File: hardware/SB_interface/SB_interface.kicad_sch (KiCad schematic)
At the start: 33 parts, among them J1 8P8C_TelPairs, J2 8P8C_TelPairs, J3 8P8C_TelPairs, J4 Screw_Terminal_01x02, J5 Screw_Terminal_01x02, J6 Conn_01x10_Pin, J7 Jack-DC, K1 J104D2C12VDC.36S, Q1 2N7002, U1 MCP23017_SP, U2 MCP23017_SP

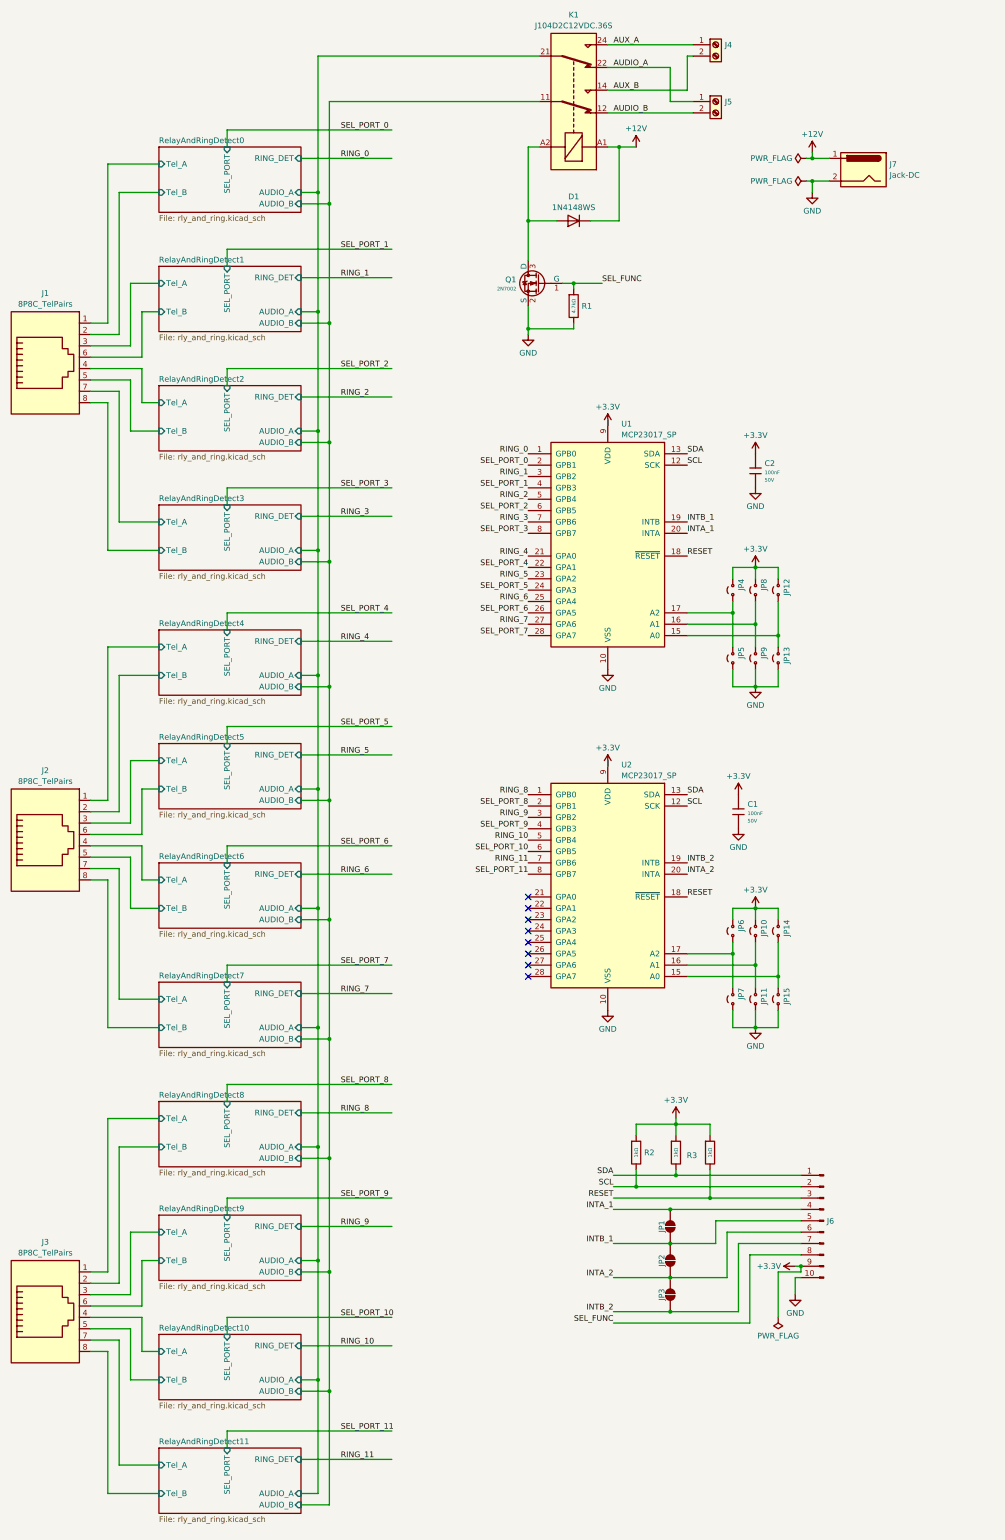
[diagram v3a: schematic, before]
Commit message: layout of tel inputs
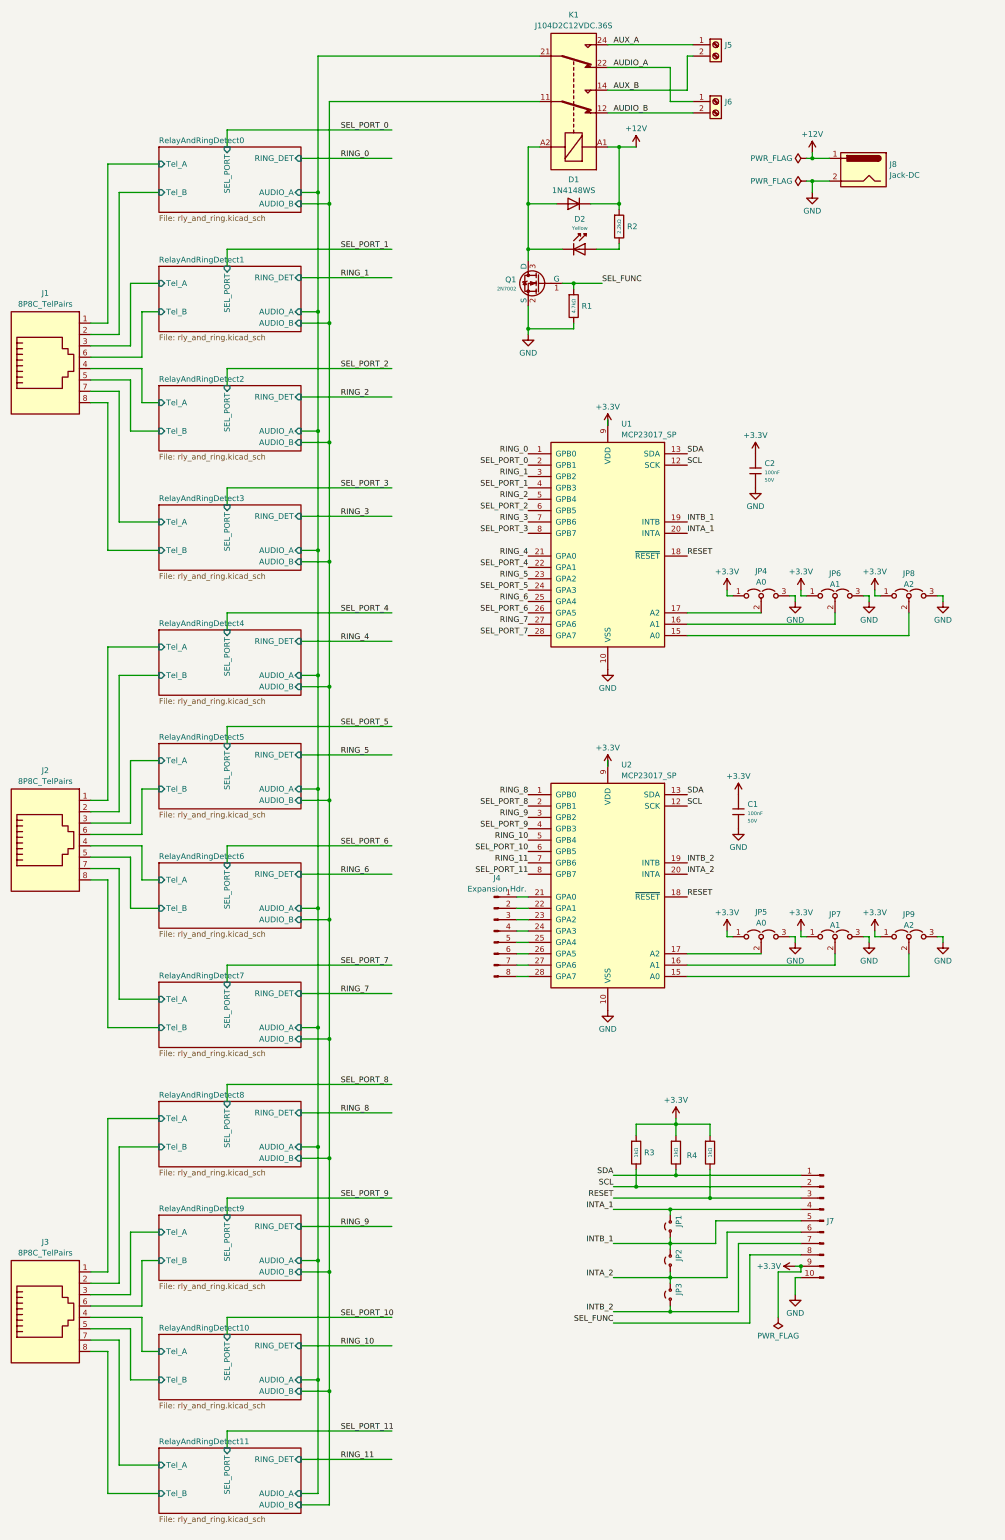
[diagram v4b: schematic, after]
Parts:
- removed JP1, JP2, JP3: SolderJumper_2_Open, Jumper:SolderJumper-2_P1.3mm_Open_Pad1.0x1.5mm, symbol Jumper:SolderJumper_2_Open
- removed JP10, JP11, JP12, JP13, JP14, JP15, JP4, JP5, JP6, JP7, JP8, JP9: Jumper_2_Small_Open, Connector_PinHeader_2.54mm:PinHeader_1x02_P2.54mm_Vertical, symbol Jumper:Jumper_2_Small_Open
- added D2: Yellow, PCM_JLCPCB:D_0805, symbol PCM_JLCPCB-Diodes:LED,0805,Yellow
- added J4: Expansion Hdr., Connector_PinHeader_2.54mm:PinHeader_1x08_P2.54mm_Vertical, symbol Connector:Conn_01x08_Pin
- added JP1, JP2, JP3: Jumper_2_Small_Open, Connector_PinHeader_2.54mm:PinHeader_1x02_P2.54mm_Vertical, symbol Jumper:Jumper_2_Small_Open
- added JP4, JP5: A0, Connector_PinHeader_2.54mm:PinHeader_1x03_P2.54mm_Vertical, symbol Jumper:Jumper_3_Open
- added JP6, JP7: A1, Connector_PinHeader_2.54mm:PinHeader_1x03_P2.54mm_Vertical, symbol Jumper:Jumper_3_Open
- added JP8, JP9: A2, Connector_PinHeader_2.54mm:PinHeader_1x03_P2.54mm_Vertical, symbol Jumper:Jumper_3_Open
- added R2: 2.2kΩ, PCM_JLCPCB:R_0805, symbol PCM_JLCPCB-Resistors:0805,2.2kΩ
- renumbered J4 to J5, J5 to J6, J6 to J7, J7 to J8, R2 to R3, R3 to R4, R4 to R5
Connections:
- net +12V: now also R2.1
- net +3.3V: now also JP4.1 (A), JP5.1 (A), JP6.1 (A), JP7.1 (A), JP8.1 (A), JP9.1 (A)
- net GND: now also JP4.3 (B), JP5.3 (B), JP6.3 (B), JP7.3 (B), JP8.3 (B), JP9.3 (B)
- net INTA_1: now also JP1.2 (B)
- net INTA_2: now also JP2.1 (A), JP3.2 (B)
- net INTB_1: now also JP1.1 (A), JP2.2 (B)
- net INTB_2: now also JP3.1 (A)
- net at U2.15 (A0): now also JP9.2 (C)
- net at U2.17 (A2): now also JP5.2 (C)
- net at D1.2 (A), K1.A2, Q1.3 (D): now also D2.1
- net at U2.16 (A1): now also JP7.2 (C)
- net at U2.21 (GPA0): now also J4.1 (Pin_1)
- net at U2.22 (GPA1): now also J4.2 (Pin_2)
- net at U2.23 (GPA2): now also J4.3 (Pin_3)
- net at U2.24 (GPA3): now also J4.4 (Pin_4)
- net at U2.25 (GPA4): now also J4.5 (Pin_5)
- net at U2.26 (GPA5): now also J4.6 (Pin_6)
- net at U2.27 (GPA6): now also J4.7 (Pin_7)
- net at U2.28 (GPA7): now also J4.8 (Pin_8)
- net at U1.15 (A0): now also JP8.2 (C)
- net at U1.17 (A2): now also JP4.2 (C)
- net at U1.16 (A1): now also JP6.2 (C)
- new net: D2.2, R2.2
- no-connect marks 8 -> 0
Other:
- moved on the sheet: D1

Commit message: more layout stuff
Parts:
- removed J4: Expansion Hdr., Connector_PinHeader_2.54mm:PinHeader_1x08_P2.54mm_Vertical, symbol Connector:Conn_01x08_Pin
- removed J7: Conn_01x10_Pin, Connector_PinHeader_2.54mm:PinHeader_1x10_P2.54mm_Vertical, symbol Connector:Conn_01x10_Pin
- removed JP1, JP2, JP3: Jumper_2_Small_Open, Connector_PinHeader_2.54mm:PinHeader_1x02_P2.54mm_Vertical, symbol Jumper:Jumper_2_Small_Open
- added J4: Conn_01x09_Pin, Connector_PinHeader_2.54mm:PinHeader_1x09_P2.54mm_Vertical, symbol Connector:Conn_01x09_Pin
- added J7: EXTENSION HDR., Connector_PinHeader_2.54mm:PinHeader_1x07_P2.54mm_Vertical, symbol Connector:Conn_01x07_Pin
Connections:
- net +3.3V: now also J4.1 (Pin_1)
- net GND: now also J4.9 (Pin_9)
- net INTA_1: now also J4.4 (Pin_4)
- net INTA_2: now also J4.8 (Pin_8)
- net INTB_1: now also J4.5 (Pin_5)
- net INTB_2: now also J4.7 (Pin_7)
- net RESET: now also J4.6 (Pin_6)
- net RING_4: now also U1.27 (GPA6); no longer U1.21 (GPA0)
- net RING_5: now also U1.25 (GPA4); no longer U1.23 (GPA2)
- net RING_6: now also U1.23 (GPA2); no longer U1.25 (GPA4)
- net RING_7: now also U1.21 (GPA0); no longer U1.27 (GPA6)
- net SCL: now also J4.2 (Pin_2)
- net SDA: now also J4.3 (Pin_3)
- net SEL_FUNC: now also U2.28 (GPA7)
- net SEL_PORT_4: now also U1.28 (GPA7); no longer U1.22 (GPA1)
- net SEL_PORT_5: now also U1.26 (GPA5); no longer U1.24 (GPA3)
- net SEL_PORT_6: now also U1.24 (GPA3); no longer U1.26 (GPA5)
- net SEL_PORT_7: now also U1.22 (GPA1); no longer U1.28 (GPA7)
- net GPA0: now reaches U2.21 (GPA0)
- net GPA0: now also J7.1 (Pin_1)
- net GPA1: now reaches U2.22 (GPA1)
- net GPA1: now also J7.2 (Pin_2)
- net GPA2: now reaches U2.23 (GPA2)
- net GPA2: now also J7.3 (Pin_3)
- net GPA3: now reaches U2.24 (GPA3)
- net GPA3: now also J7.4 (Pin_4)
- net GPA4: now reaches U2.25 (GPA4)
- net GPA4: now also J7.5 (Pin_5)
- net GPA5: now reaches U2.26 (GPA5)
- net GPA5: now also J7.6 (Pin_6)
- net GPA6: now reaches U2.27 (GPA6)
- net GPA6: now also J7.7 (Pin_7)
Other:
- moved on the sheet: R3, R4

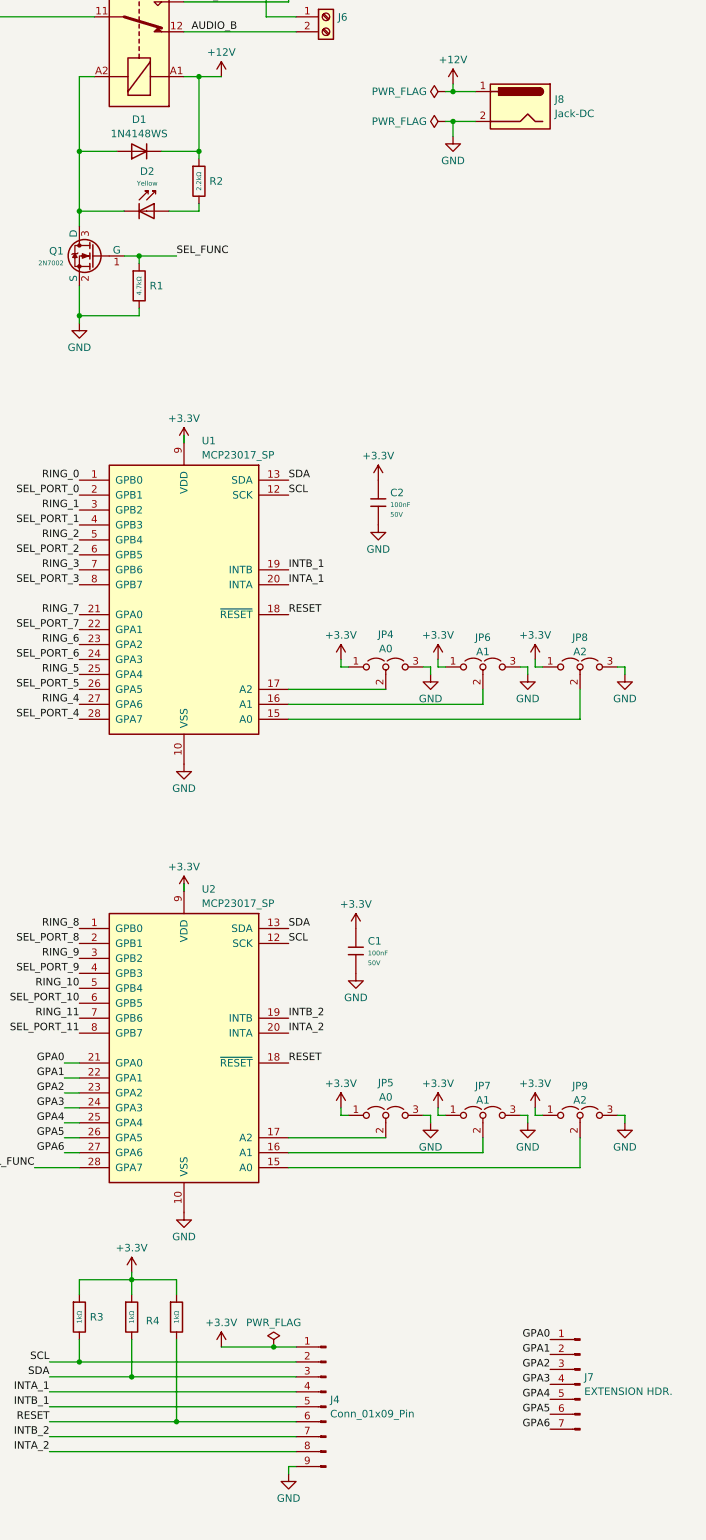
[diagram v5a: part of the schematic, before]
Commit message: added prototyping area
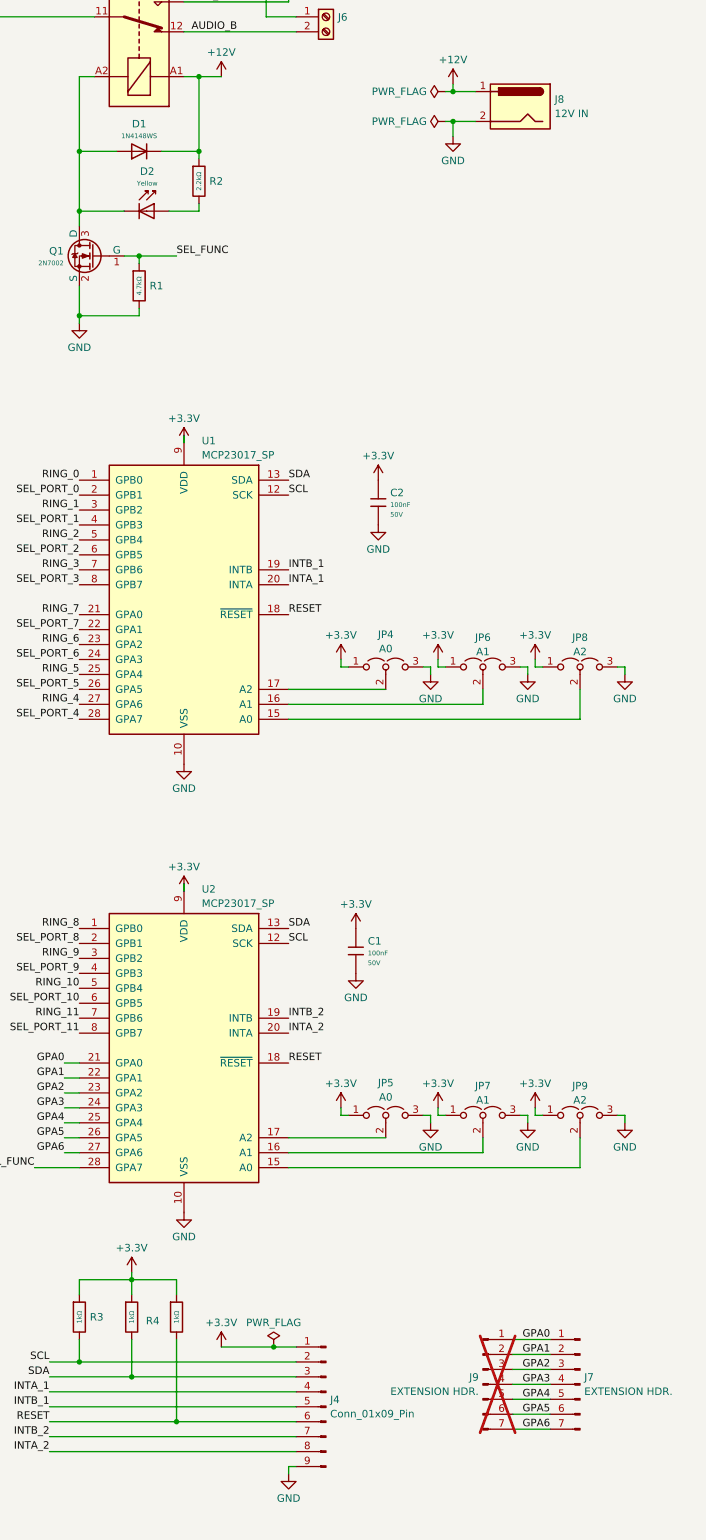
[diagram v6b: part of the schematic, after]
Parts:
- removed D1: 1N4148WS, Diode_SMD:D_SOD-323, symbol Diode:1N4148WS
- added D1: 1N4148WS, PCM_JLCPCB:D_SOD-323, symbol PCM_JLCPCB-Diodes:Switching,1N4148WS
- added J9: EXTENSION HDR., Connector_PinHeader_2.54mm:PinHeader_1x07_P2.54mm_Vertical, symbol Connector:Conn_01x07_Pin
- J5: value Screw_Terminal_01x02 -> AUX
- J6: value Screw_Terminal_01x02 -> AUDIO
- J8: value Jack-DC -> 12V IN
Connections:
- net +12V: now also D1.1
- net GPA0: now also J9.1 (Pin_1)
- net GPA1: now also J9.2 (Pin_2)
- net GPA2: now also J9.3 (Pin_3)
- net GPA3: now also J9.4 (Pin_4)
- net GPA4: now also J9.5 (Pin_5)
- net GPA5: now also J9.6 (Pin_6)
- net GPA6: now also J9.7 (Pin_7)
- net at D2.1, K1.A2, Q1.3 (D): now also D1.2
